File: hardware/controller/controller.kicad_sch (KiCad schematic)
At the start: 28 parts, among them J1 Conn_02x15_Odd_Even, J10 conn_wifi, J11 conn_gpio, J2 Conn_01x20, J3 Conn_01x20, J4 Conn_01x02, J5 conn_vol, J6 conn_bl, J7 conn_br, J8 conn_dsp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

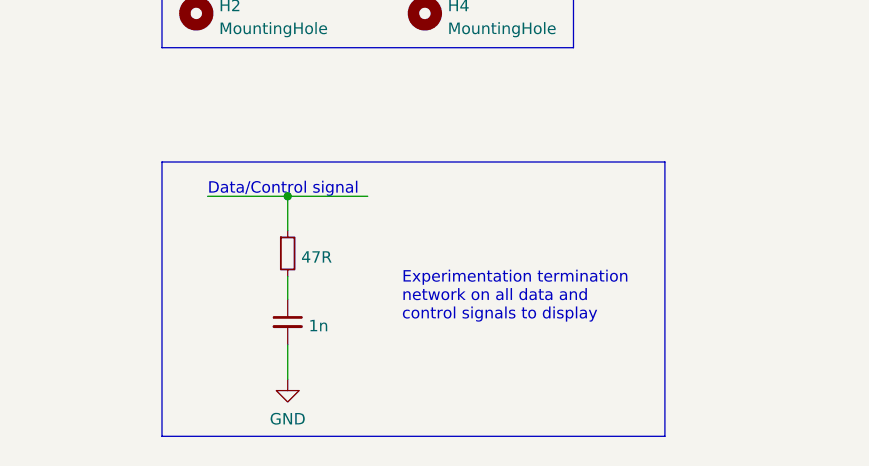
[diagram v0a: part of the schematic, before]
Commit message: Removed experimental termination as it is not required
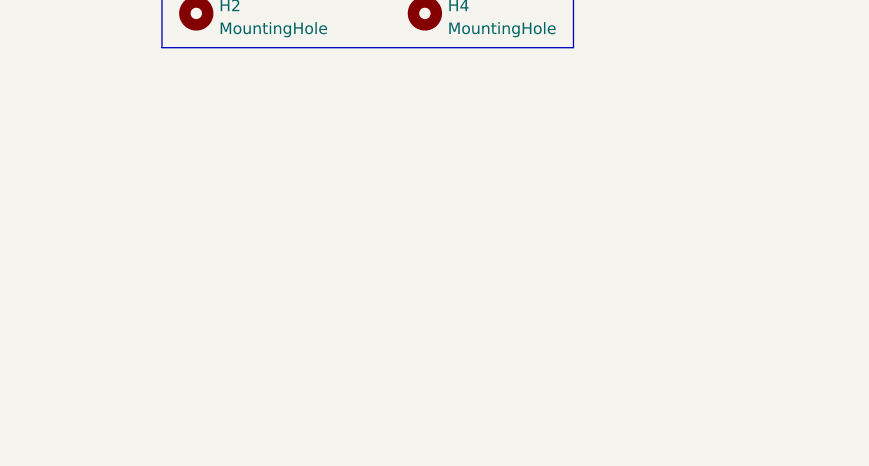
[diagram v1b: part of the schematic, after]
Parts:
- removed #C?: 1n, symbol Device:C_Small
- removed #R?: 47R, symbol Device:R_Small
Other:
- note removed: "Data/Control signal"
- note removed: "Experimentation termination network on all data and control signals to display"
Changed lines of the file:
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@@
   (junction (at 234.95 62.23) (diameter 0) (color 0 0 0 0)
-  )
-  (junction (at 228.6 246.38) (diameter 0) (color 0 0 0 0)
   )
   (junction (at 250.19 100.33) (diameter 0) (color 0 0 0 0)
@@
     (stroke (width 0) (type default) (color 0 0 0 0))
   )
-  (wire (pts (xy 228.6 246.38) (xy 237.49 246.38))
-    (stroke (width 0) (type default) (color 0 0 0 0))
-  )
   (wire (pts (xy 317.5 90.17) (xy 328.93 90.17))
     (stroke (width 0) (type default) (color 0 0 0 0))
@@
     (stroke (width 0) (type default) (color 0 0 0 0))
   )
-  (wire (pts (xy 228.6 262.89) (xy 228.6 266.7))
-    (stroke (width 0) (type default) (color 0 0 0 0))
-  )
   (wire (pts (xy 144.78 259.08) (xy 144.78 260.35))
     (stroke (width 0) (type default) (color 0 0 0 0))
@@
   )
   (wire (pts (xy 85.09 175.26) (xy 85.09 185.42))
-    (stroke (width 0) (type default) (color 0 0 0 0))
-  )
-  (polyline (pts (xy 270.51 242.57) (xy 270.51 273.05))
     (stroke (width 0) (type default) (color 0 0 0 0))
   )
@@
     (stroke (width 0) (type default) (color 255 0 255 1))
   )
-  (polyline (pts (xy 214.63 242.57) (xy 270.51 242.57))
-    (stroke (width 0) (type default) (color 0 0 0 0))
-  )
   (wire (pts (xy 74.93 243.84) (xy 74.93 260.35))
     (stroke (width 0) (type default) (color 0 0 0 0))
@@
     (stroke (width 0) (type default) (color 0 0 0 0))
   )
-  (polyline (pts (xy 270.51 273.05) (xy 214.63 273.05))
-    (stroke (width 0) (type default) (color 0 0 0 0))
-  )
   (wire (pts (xy 58.42 83.82) (xy 58.42 96.52))
     (stroke (width 0) (type default) (color 0 0 0 0))
@@
   )
   (wire (pts (xy 325.12 185.42) (xy 346.71 185.42))
-    (stroke (width 0) (type default) (color 0 0 0 0))
-  )
-  (polyline (pts (xy 214.63 242.57) (xy 214.63 273.05))
     (stroke (width 0) (type default) (color 0 0 0 0))
   )
@@
     (stroke (width 0) (type default) (color 0 0 0 0))
   )
-  (wire (pts (xy 228.6 246.38) (xy 228.6 250.19))
-    (stroke (width 0) (type default) (color 0 0 0 0))
-  )
   (wire (pts (xy 43.18 83.82) (xy 43.18 96.52))
     (stroke (width 0) (type default) (color 0 0 0 0))
@@
     (stroke (width 0) (type default) (color 0 0 0 0))
   )
-  (wire (pts (xy 228.6 255.27) (xy 228.6 257.81))
-    (stroke (width 0) (type default) (color 0 0 0 0))
-  )
   (wire (pts (xy 92.71 156.21) (xy 92.71 166.37))
     (stroke (width 0) (type default) (color 0 0 0 0))
@@
   )
   (polyline (pts (xy 281.94 53.34) (xy 281.94 69.85))
-    (stroke (width 0) (type default) (color 0 0 0 0))
-  )
-  (wire (pts (xy 219.71 246.38) (xy 228.6 246.38))
     (stroke (width 0) (type default) (color 0 0 0 0))
   )
@@
     (effects (font (size 1.27 1.27)) (justify left bottom))
   )
-  (text "Data/Control signal" (at 219.71 246.38 0)
-    (effects (font (size 1.27 1.27)) (justify left bottom))
-  )
   (text "Open Source\nHardware" (at 396.24 262.89 0)
     (effects (font (size 1.27 1.27)) (justify left bottom))
@@
   )
   (text "PICO MCU\n" (at 19.05 115.57 0)
-    (effects (font (size 1.27 1.27)) (justify left bottom))
-  )
-  (text "Experimentation termination\nnetwork on all data and \ncontrol signals to display"
-    (at 241.3 260.35 0)
     (effects (font (size 1.27 1.27)) (justify left bottom))
   )
@@
     (pin "1")
   )
-  (symbol (lib_id "power:GND") (at 228.6 266.7 0) (unit 1)
-    (in_bom yes) (on_board yes) (fields_autoplaced)
-    (property "Reference" "#PWR?" (id 0) (at 228.6 273.05 0)
-      (effects (font (size 1.27 1.27)) hide)
-    )
-    (property "Value" "GND" (id 1) (at 228.6 271.1434 0))
-    (property "Footprint" "" (id 2) (at 228.6 266.7 0)
-      (effects (font (size 1.27 1.27)) hide)
-    )
-    (property "Datasheet" "" (id 3) (at 228.6 266.7 0)
-      (effects (font (size 1.27 1.27)) hide)
-    )
-    (pin "1")
-  )
   (symbol (lib_id "power:+3.3V") (at 194.31 62.23 0) (unit 1)
     (in_bom yes) (on_board yes) (fields_autoplaced)
@@
     )
     (pin "1")
-  )
-  (symbol (lib_id "Device:C_Small") (at 228.6 260.35 0) (unit 1)
-    (in_bom yes) (on_board yes) (fields_autoplaced)
-    (property "Reference" "#C?" (id 0) (at 230.9241 259.5216 0)
-      (effects (font (size 1.27 1.27)) (justify left) hide)
-    )
-    (property "Value" "1n" (id 1) (at 230.9241 260.7901 0)
-      (effects (font (size 1.27 1.27)) (justify left))
-    )
-    (property "Footprint" "" (id 2) (at 228.6 260.35 0)
-      (effects (font (size 1.27 1.27)) hide)
-    )
-    (property "Datasheet" "~" (id 3) (at 228.6 260.35 0)
-      (effects (font (size 1.27 1.27)) hide)
-    )
-    (pin "1")
-    (pin "2")
   )
   (symbol (lib_id "project:+3V3_DISPLAY") (at 31.75 44.45 90) (unit 1)
@@
     )
     (pin "1")
-  )
-  (symbol (lib_id "Device:R_Small") (at 228.6 252.73 0) (unit 1)
-    (in_bom yes) (on_board yes) (fields_autoplaced)
-    (property "Reference" "#R?" (id 0) (at 230.0986 251.8953 0)
-      (effects (font (size 1.27 1.27)) (justify left) hide)
-    )
-    (property "Value" "47R" (id 1) (at 230.0986 253.1638 0)
-      (effects (font (size 1.27 1.27)) (justify left))
-    )
-    (property "Footprint" "" (id 2) (at 228.6 252.73 0)
-      (effects (font (size 1.27 1.27)) hide)
-    )
-    (property "Datasheet" "~" (id 3) (at 228.6 252.73 0)
-      (effects (font (size 1.27 1.27)) hide)
-    )
-    (pin "1")
-    (pin "2")
   )
   (symbol (lib_id "project:Display_5{dblquote}_RA8875") (at 60.96 55.88 0) (unit 1)
@@
   )
   (symbol_instances
-    (path "/af1102d8-3fca-4528-ae86-8b51184d5f5e"
-      (reference "#C?") (unit 1) (value "1n") (footprint "")
-    )
     (path "/996a8dc6-561a-443a-8843-e688e3bd2e77"
       (reference "#FLG01") (unit 1) (value "PWR_FLAG") (footprint "")
@@
       (reference "#PWR?") (unit 1) (value "GND") (footprint "")
     )
-    (path "/7ed4ef6f-5219-410b-a78f-a27322c389cf"
-      (reference "#PWR?") (unit 1) (value "GND") (footprint "")
-    )
-    (path "/f482f350-a5ad-43b8-9ec2-07fb6ee67689"
-      (reference "#R?") (unit 1) (value "47R") (footprint "")
-    )
     (path "/02a22cc8-7c94-420b-8aaa-b9d35bfadbc7"

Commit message: Added  annotation
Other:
- note added: "ADDR0"
- note added: "ADDR1"
- note added: "ADDR2"
- note added: "MUX_EN"
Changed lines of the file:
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@@
     (stroke (width 0) (type default) (color 0 0 0 0))
+  )
+  (polyline (pts (xy 148.59 22.86) (xy 148.59 25.4))
+    (stroke (width 0) (type default) (color 255 0 0 1))
   )
   (polyline (pts (xy 114.3 16.51) (xy 180.34 16.51))
@@
     (stroke (width 0) (type default) (color 0 0 0 0))
   )
-  (polyline (pts (xy 144.78 25.4) (xy 177.8 25.4))
+  (polyline (pts (xy 144.78 22.86) (xy 177.8 22.86))
     (stroke (width 0) (type default) (color 255 0 0 1))
   )
@@
     (stroke (width 0) (type default) (color 0 0 0 0))
   )
-  (polyline (pts (xy 177.8 25.4) (xy 177.8 21.59))
+  (polyline (pts (xy 177.8 22.86) (xy 177.8 19.05))
     (stroke (width 0) (type default) (color 255 0 0 1))
   )
@@
     (stroke (width 0) (type default) (color 0 0 0 0))
   )
-  (polyline (pts (xy 144.78 21.59) (xy 177.8 21.59))
+  (polyline (pts (xy 144.78 19.05) (xy 177.8 19.05))
     (stroke (width 0) (type default) (color 255 0 0 1))
   )
@@
     (stroke (width 0) (type default) (color 255 0 0 1))
   )
-  (polyline (pts (xy 144.78 21.59) (xy 144.78 25.4))
+  (polyline (pts (xy 144.78 19.05) (xy 144.78 22.86))
     (stroke (width 0) (type default) (color 255 0 0 1))
   )
@@
     (effects (font (size 1.27 1.27)) (justify left bottom))
   )
+  (text "MUX_EN" (at 151.13 85.09 90)
+    (effects (font (size 1.27 1.27)) (justify left bottom))
+  )
   (text "Open Source\nHardware" (at 396.24 262.89 0)
     (effects (font (size 1.27 1.27)) (justify left bottom))
@@
     (effects (font (size 1.27 1.27)) (justify left bottom))
   )
+  (text "ADDR1" (at 153.67 83.82 90)
+    (effects (font (size 1.27 1.27)) (justify left bottom))
+  )
   (text "Buttons \nRight\n" (at 350.52 135.89 0)
     (effects (font (size 1.27 1.27)) (justify left bottom))
@@
     (effects (font (size 1.27 1.27)) (justify left bottom))
   )
-  (text "Correction to activate backlight" (at 146.05 24.13 0)
+  (text "Correction to activate backlight" (at 146.05 21.59 0)
     (effects (font (size 1.27 1.27)) (justify left bottom))
   )
@@
   )
   (text "PICO MCU\n" (at 19.05 115.57 0)
+    (effects (font (size 1.27 1.27)) (justify left bottom))
+  )
+  (text "ADDR0" (at 153.67 29.21 90)
     (effects (font (size 1.27 1.27)) (justify left bottom))
   )
@@
     (effects (font (size 1.27 1.27) (thickness 0.254) bold italic) (justify left bottom))
   )
+  (text "ADDR2" (at 151.13 29.21 90)
+    (effects (font (size 1.27 1.27)) (justify left bottom))
+  )
   (label "DI.DATA0" (at 43.18 27.94 90)

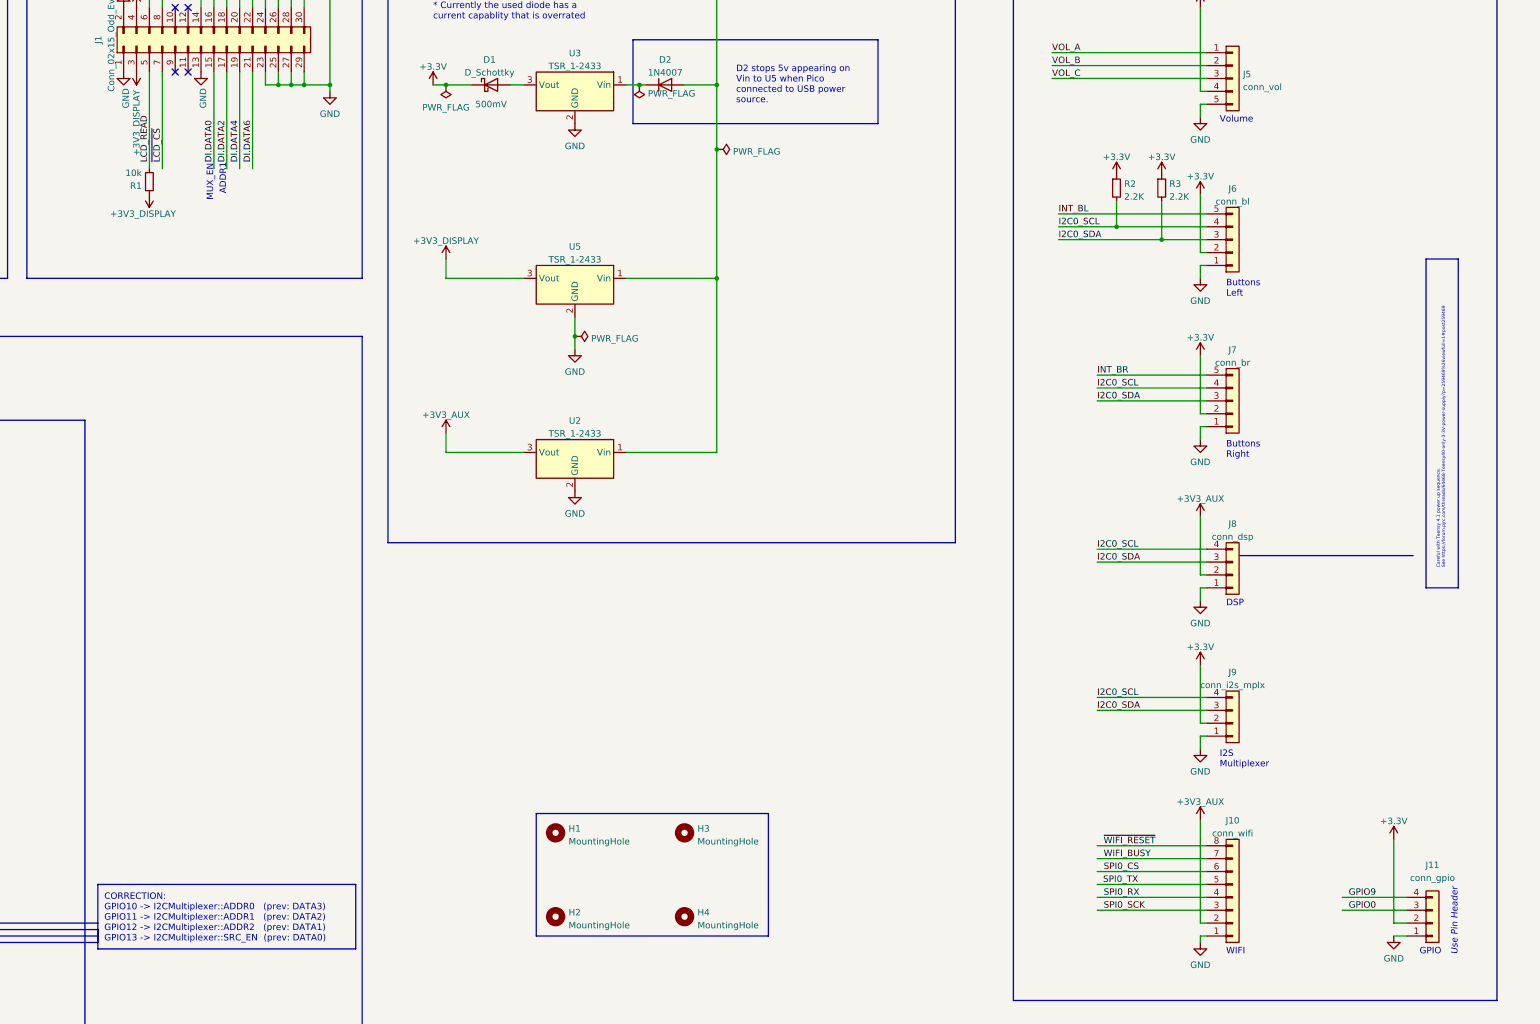
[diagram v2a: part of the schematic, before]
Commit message: Small changes to controller circuit
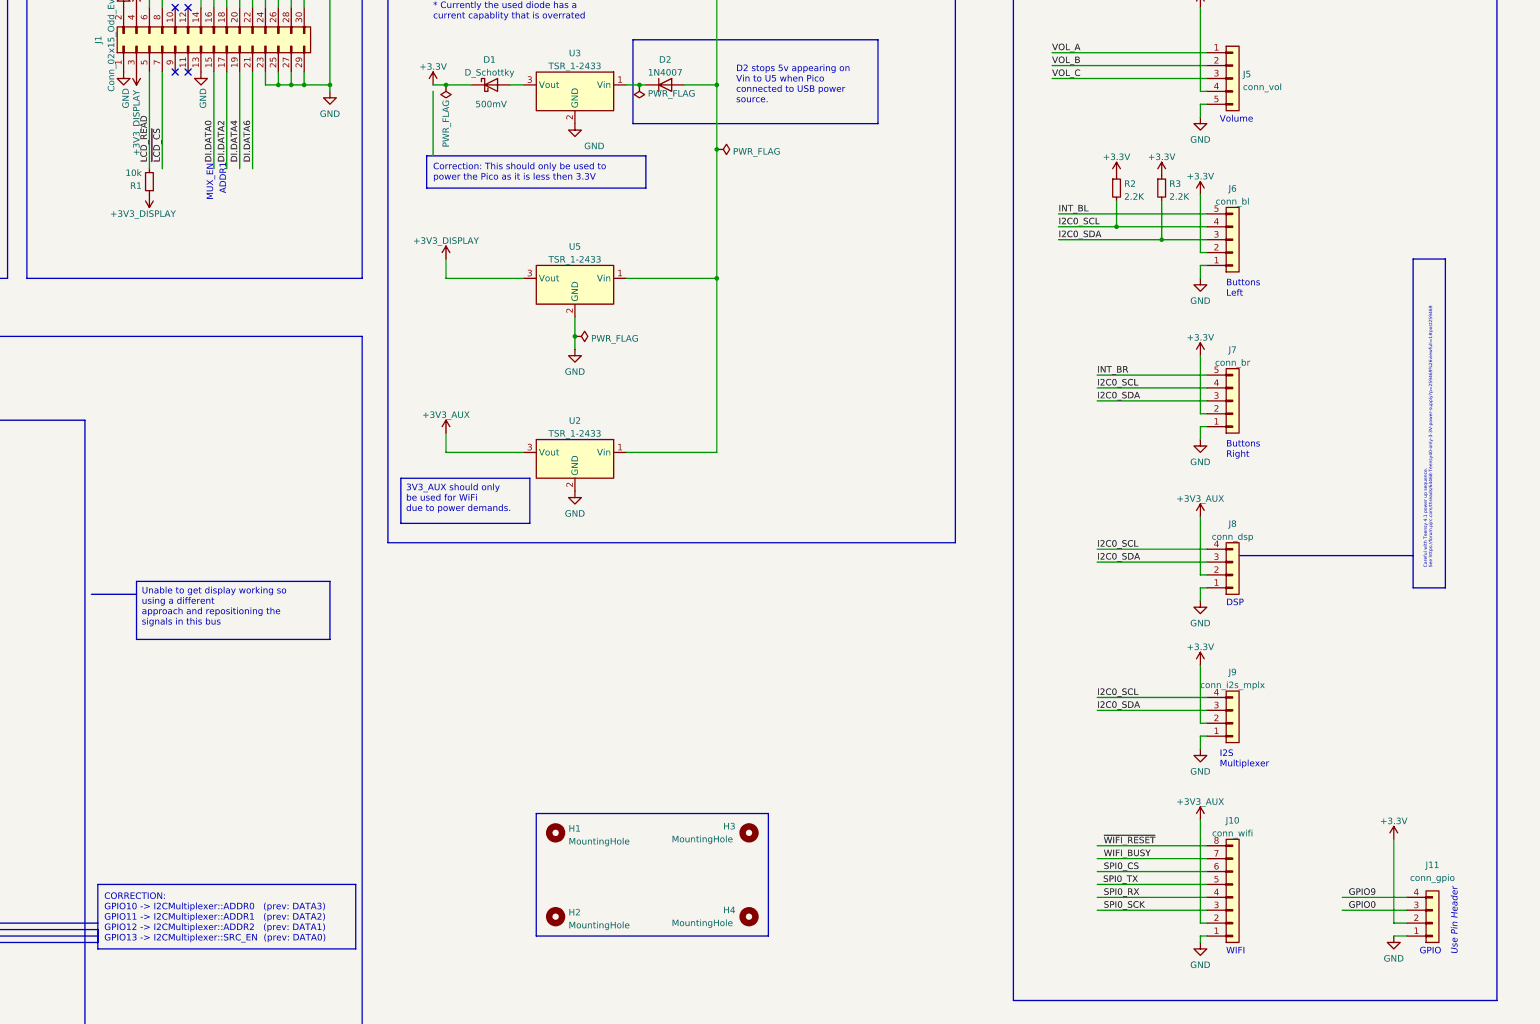
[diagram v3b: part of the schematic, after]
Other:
- note added: "Correction: This should only be used to power the Pico as it is less then 3.3V"
- moved on the sheet: H3, H4

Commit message: Keep up to date with actual circuit
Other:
- note added: "Connected to button bank"
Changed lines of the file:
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@@
+    (stroke (width 0) (type default))
+  )
+  (polyline (pts (xy 355.6 92.71) (xy 363.22 92.71))
     (stroke (width 0) (type default))
   )
@@
     (stroke (width 0) (type default) (color 255 0 0 1))
   )
+  (rectangle (start 363.22 88.9) (end 378.46 95.25)
+    (stroke (width 0) (type default))
+    (fill (type none))
+  )
   (text_box "3V3_AUX should only be used for WiFi \ndue to power demands. "
     (at 187.96 139.7 0) (size 25.4 8.89)
@@
     (effects (font (size 1.27 1.27)) (justify left bottom))
   )
+  (text "Connected to  \nbutton bank" (at 364.49 93.98 0)
+    (effects (font (size 1.27 1.27)) (justify left bottom))
+  )

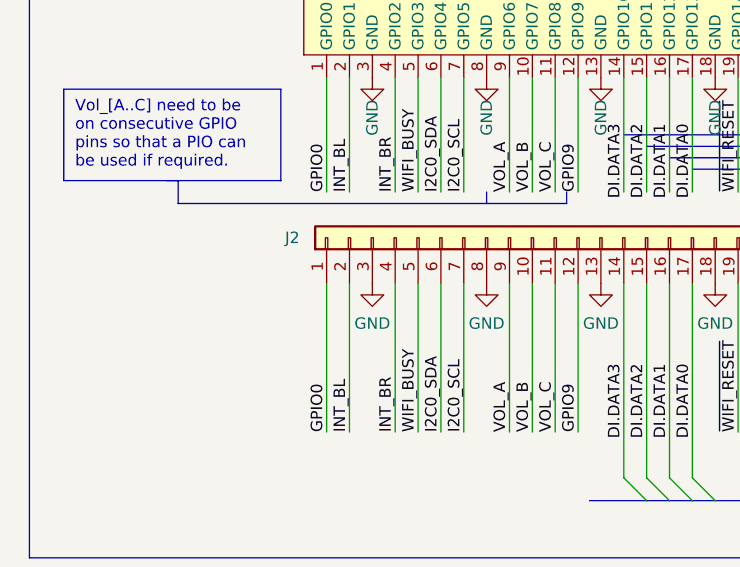
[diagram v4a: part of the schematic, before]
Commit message: GPIO currently used for UART1 documented
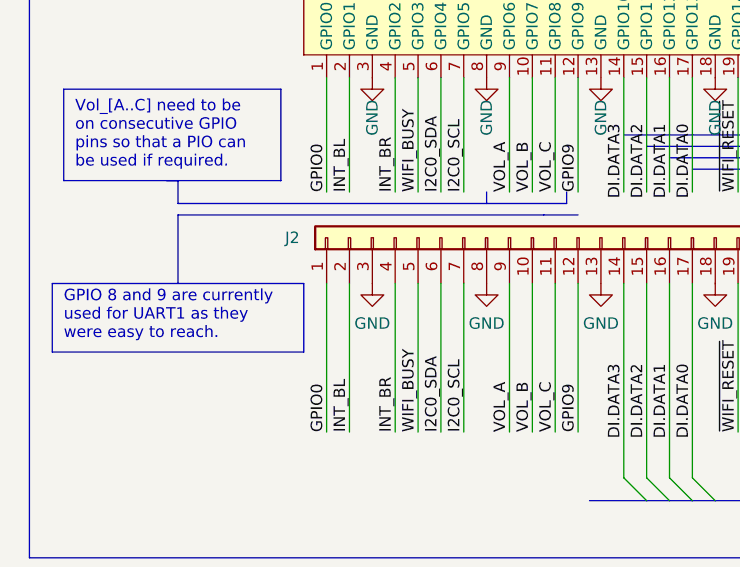
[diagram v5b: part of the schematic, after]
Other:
- note added: "GPIO 8 and 9 are currently used for UART1 as they were easy to reach."
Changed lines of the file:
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@@
+    (stroke (width 0) (type default))
+  )
+  (polyline (pts (xy 16.51 243.84) (xy 44.45 243.84))
     (stroke (width 0) (type default))
   )
@@
     (stroke (width 0) (type default))
   )
+  (polyline (pts (xy 71.12 236.22) (xy 30.48 236.22))
+    (stroke (width 0) (type default))
+  )
   (bus (pts (xy 87.63 267.97) (xy 90.17 267.97))
     (stroke (width 0) (type default))
@@
   )
   (wire (pts (xy 87.63 54.61) (xy 102.87 54.61))
+    (stroke (width 0) (type default))
+  )
+  (polyline (pts (xy 30.48 236.22) (xy 30.48 243.84))
     (stroke (width 0) (type default))
   )
@@
     (stroke (width 0) (type default))
   )
+  (polyline (pts (xy 16.51 243.84) (xy 16.51 251.46))
+    (stroke (width 0) (type default))
+  )
   (polyline (pts (xy 64.77 233.68) (xy 64.77 234.95))
     (stroke (width 0) (type default))
@@
   )
   (wire (pts (xy 62.23 175.26) (xy 62.23 185.42))
+    (stroke (width 0) (type default))
+  )
+  (polyline (pts (xy 44.45 243.84) (xy 44.45 251.46))
     (stroke (width 0) (type default))
   )
@@
     (stroke (width 0) (type default))
   )
+  (polyline (pts (xy 44.45 251.46) (xy 16.51 251.46))
+    (stroke (width 0) (type default))
+  )
   (wire (pts (xy 325.12 119.38) (xy 346.71 119.38))
     (stroke (width 0) (type default))
@@
   )
   (wire (pts (xy 325.12 156.21) (xy 346.71 156.21))
+    (stroke (width 0) (type default))
+  )
+  (polyline (pts (xy 71.12 236.22) (xy 74.93 236.22))
     (stroke (width 0) (type default))
   )
@@
     (effects (font (size 1.27 1.27)) (justify left bottom))
   )
+  (text "GPIO 8 and 9 are currently \nused for UART1 as they \nwere easy to reach."
+    (at 17.78 250.19 0)
+    (effects (font (size 1.27 1.27)) (justify left bottom))
+  )
